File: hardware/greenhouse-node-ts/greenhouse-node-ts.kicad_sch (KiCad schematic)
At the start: 31 parts, among them J1 Conn_01x12_Male, J3 Conn_01x02_Pin, J7 Conn_01x04_Pin, SW1 SW_Push, U5 STM32F030F4P6, U7 PCF8574ATS/3,118, U8 XC6706x, U9 RFM69HW

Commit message: Tweaks to nodes
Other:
- moved on the sheet: AE1, C1, C10, C13, C14, C15, C16, D10, D6, D7, D8, D9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

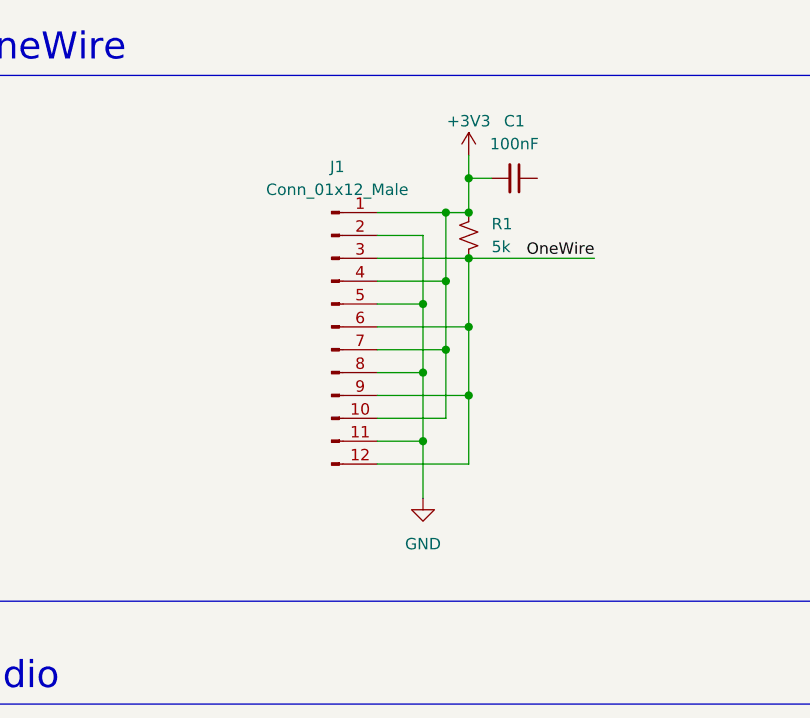
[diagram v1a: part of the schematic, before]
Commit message: Fixed cap sizes, generated BOMs
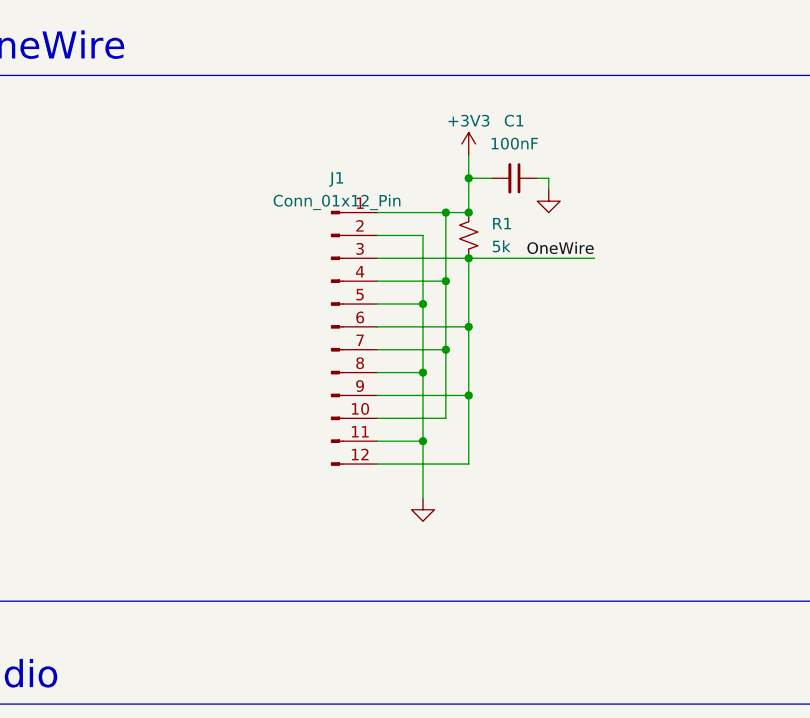
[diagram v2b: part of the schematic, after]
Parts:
- C14, C16: footprint Capacitor_THT:C_Disc_D4.7mm_W2.5mm_P5.00mm -> Capacitor_THT:C_Disc_D3.0mm_W2.0mm_P2.50mm
- J1: value Conn_01x12_Male -> Conn_01x12_Pin; footprint Connector_JST:JST_PH_B12B-PH-K_1x12_P2.00mm_Vertical -> (none); symbol Connector:Conn_01x12_Male -> Connector:Conn_01x12_Pin
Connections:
- net GND: now also C1.1
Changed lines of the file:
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@@
+    (stroke (width 0) (type default))
+  )
+  (wire (pts (xy 287.02 64.77) (xy 287.02 66.04))
     (stroke (width 0) (type default))
   )
@@
   )
   (wire (pts (xy 294.64 146.05) (xy 285.75 146.05))
+    (stroke (width 0) (type default))
+  )
+  (wire (pts (xy 285.75 64.77) (xy 287.02 64.77))
     (stroke (width 0) (type default))
   )
@@
     )
   )
-  (symbol (lib_id "power:GND") (at 273.05 100.33 0) (unit 1)
+  (symbol (lib_id "Nick:GND") (at 273.05 100.33 0) (unit 1)
     (in_bom yes) (on_board yes) (dnp no) (fields_autoplaced)
     (property "Reference" "#PWR01" (at 273.05 106.68 0)
@@
     )
     (property "Value" "GND" (at 273.05 105.41 0)
-      (effects (font (size 1.27 1.27)))
+      (effects (font (size 1.27 1.27)) hide)
     )
     (property "Footprint" "" (at 273.05 100.33 0)
@@
       (effects (font (size 1.27 1.27)))
     )
-    (property "Footprint" "Capacitor_THT:C_Disc_D4.7mm_W2.5mm_P5.00mm" (at 166.37 142.24 0)
+    (property "Footprint" "Capacitor_THT:C_Disc_D3.0mm_W2.0mm_P2.50mm" (at 166.37 142.24 0)
       (effects (font (size 1.27 1.27)) hide)
     )
@@
         (path "/d6d8dcc8-67cc-42c5-89b4-d76037b5248a"
           (reference "H4") (unit 1)
+        )
+      )
+    )
+  )
+  (symbol (lib_id "Nick:GND") (at 287.02 66.04 0) (unit 1)
+    (in_bom yes) (on_board yes) (dnp no) (fields_autoplaced)
+    (property "Reference" "#PWR05" (at 287.02 72.39 0)
+      (effects (font (size 1.27 1.27)) hide)
+    )
+    (property "Value" "GND" (at 287.02 71.12 0)
+      (effects (font (size 1.27 1.27)) hide)
+    )
+    (property "Footprint" "" (at 287.02 66.04 0)
+      (effects (font (size 1.27 1.27)) hide)
+    )
+    (property "Datasheet" "" (at 287.02 66.04 0)
+      (effects (font (size 1.27 1.27)) hide)
+    )
+    (pin "1")
+    (instances
+      (project "greenhouse-node-ts"
+        (path "/d6d8dcc8-67cc-42c5-89b4-d76037b5248a"
+          (reference "#PWR05") (unit 1)
         )
       )
@@
     )
   )
-  (symbol (lib_id "power:GND") (at 297.18 143.51 0) (unit 1)
+  (symbol (lib_id "Nick:GND") (at 297.18 143.51 0) (unit 1)
     (in_bom yes) (on_board yes) (dnp no) (fields_autoplaced)
     (property "Reference" "#PWR030" (at 297.18 149.86 0)
@@
       (effects (font (size 1.27 1.27)) hide)
     )
-    (property "Value" "GND" (at 124.46 231.1399 0)
-      (effects (font (size 1.27 1.27)) (justify left) hide)
+    (property "Value" "GND" (at 121.92 234.95 0)
+      (effects (font (size 1.27 1.27)) hide)
     )
     (property "Footprint" "" (at 121.92 229.87 0)
@@
       (effects (font (size 1.27 1.27)))
     )
-    (property "Footprint" "Capacitor_THT:C_Disc_D4.7mm_W2.5mm_P5.00mm" (at 266.7 137.16 0)
+    (property "Footprint" "Capacitor_THT:C_Disc_D3.0mm_W2.0mm_P2.50mm" (at 266.7 137.16 0)
       (effects (font (size 1.27 1.27)) hide)
     )
@@
     )
   )
-  (symbol (lib_id "Connector:Conn_01x12_Male") (at 262.89 81.28 0) (unit 1)
-    (in_bom yes) (on_board yes) (dnp no) (fields_autoplaced)
-    (property "Reference" "J1" (at 263.525 63.5 0)
-      (effects (font (size 1.27 1.27)))
-    )
-    (property "Value" "Conn_01x12_Male" (at 263.525 66.04 0)
-      (effects (font (size 1.27 1.27)))
-    )
-    (property "Footprint" "Connector_JST:JST_PH_B12B-PH-K_1x12_P2.00mm_Vertical" (at 262.89 81.28 0)
-      (effects (font (size 1.27 1.27)) hide)
-    )
+  (symbol (lib_id "Connector:Conn_01x12_Pin") (at 262.89 81.28 0) (unit 1)
+    (in_bom yes) (on_board yes) (dnp no) (fields_autoplaced)
+    (property "Reference" "J1" (at 263.525 64.77 0)
+      (effects (font (size 1.27 1.27)))
+    )
+    (property "Value" "Conn_01x12_Pin" (at 263.525 67.31 0)
+      (effects (font (size 1.27 1.27)))
+    )
+    (property "Footprint" "" (at 262.89 81.28 0)
+      (effects (font (size 1.27 1.27)) hide)
+    )

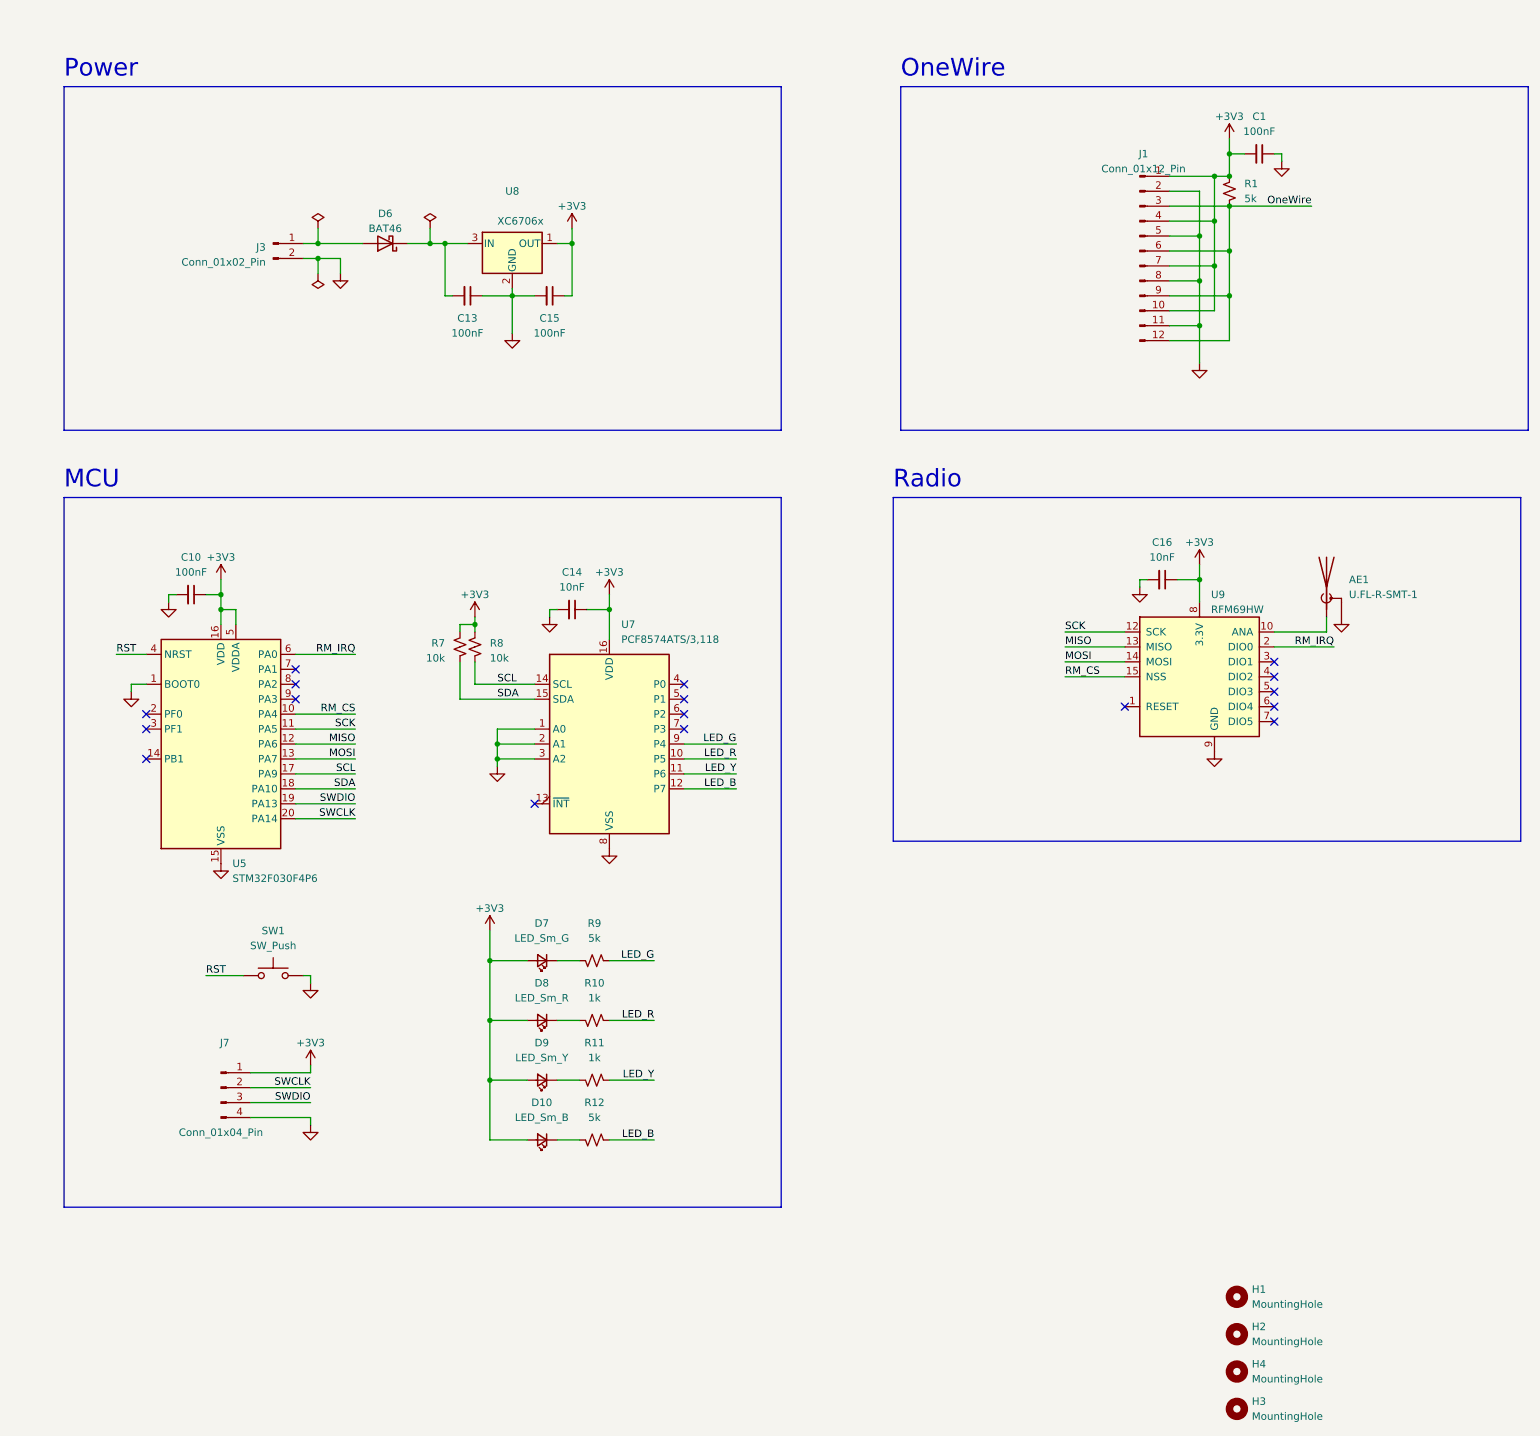
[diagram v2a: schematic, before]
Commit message: Improved schematics
Add todos, test points, fixed PCF8574 symbol,
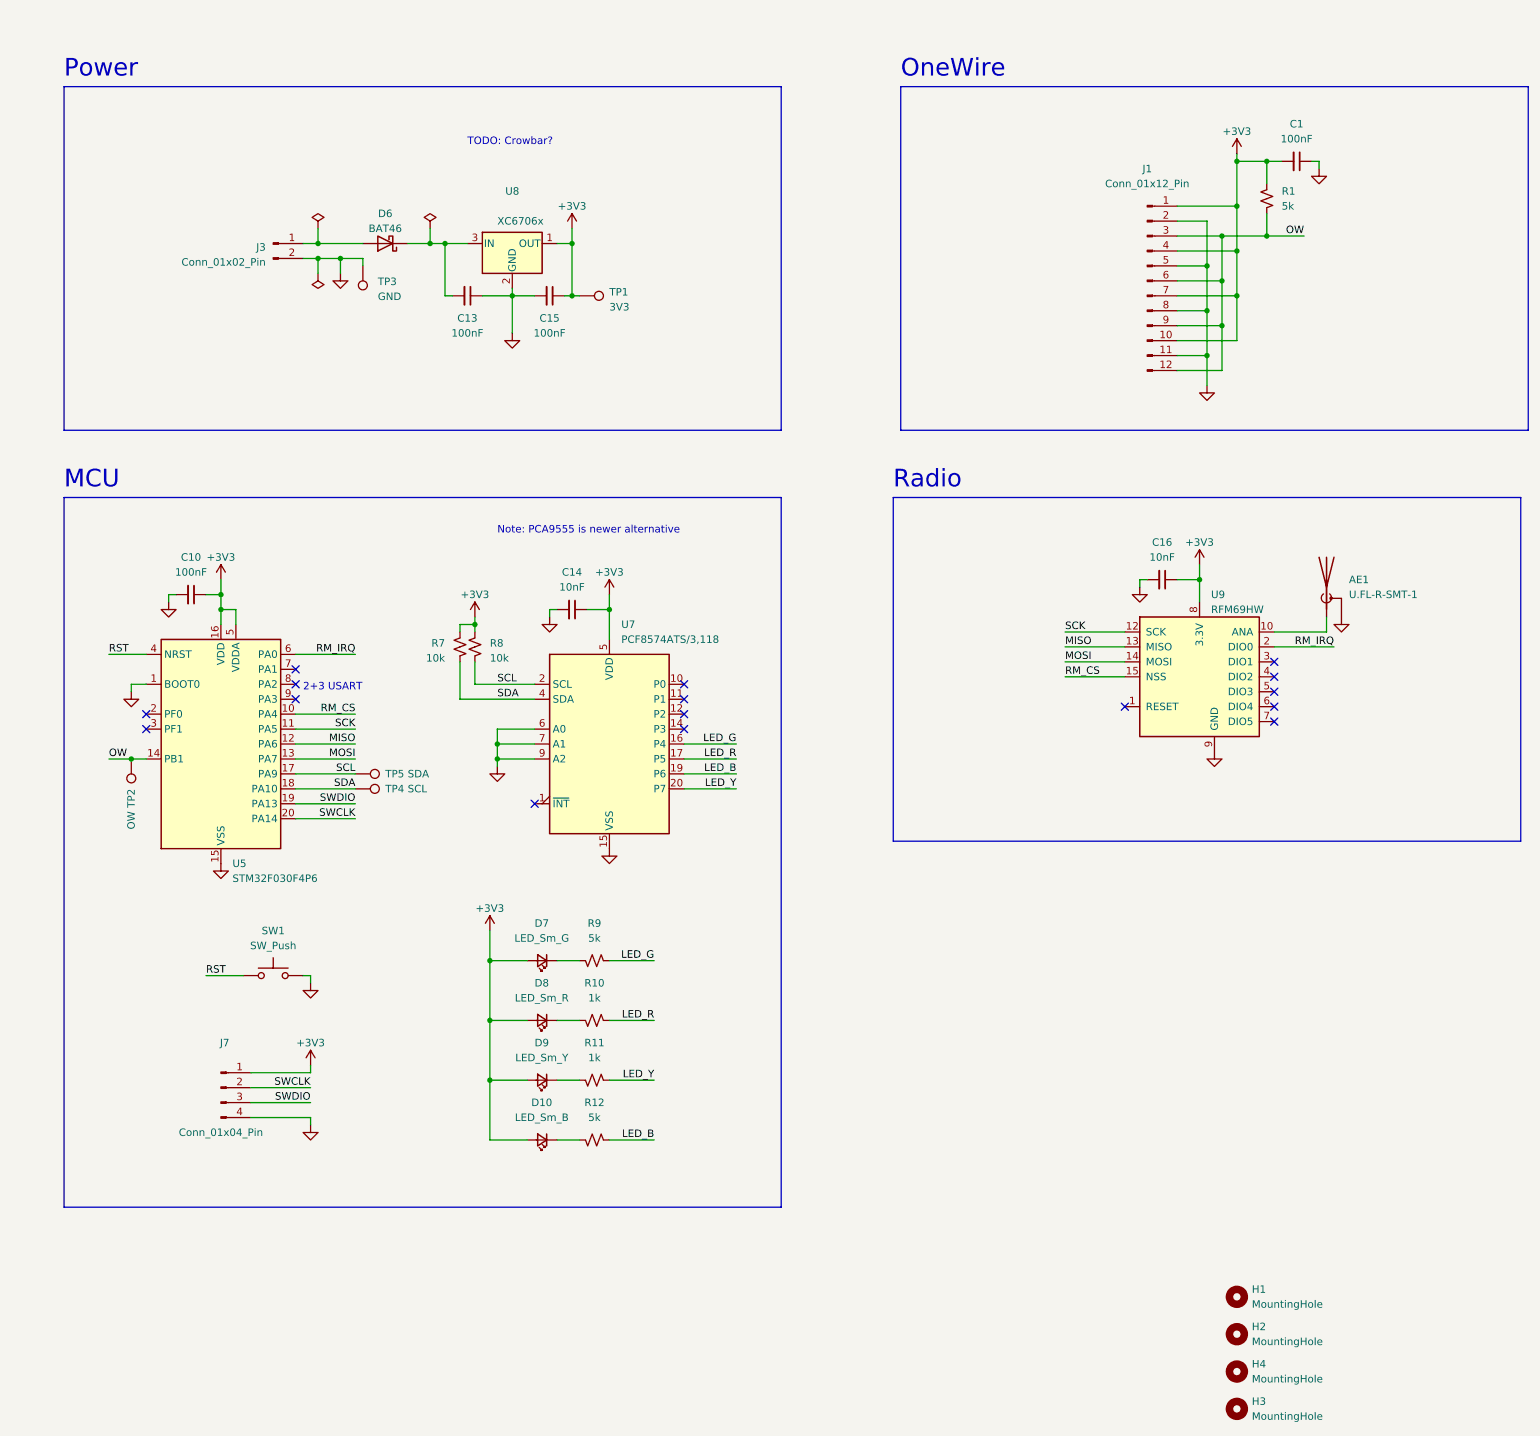
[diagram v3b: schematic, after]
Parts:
- added TP1: 3V3, TestPoint:TestPoint_Keystone_5019_Minature, symbol Connector:TestPoint
- added TP2: OW, TestPoint:TestPoint_Keystone_5019_Minature, symbol Connector:TestPoint
- added TP3: GND, TestPoint:TestPoint_Keystone_5019_Minature, symbol Connector:TestPoint
- added TP4: SCL, TestPoint:TestPoint_Keystone_5019_Minature, symbol Connector:TestPoint
- added TP5: SDA, TestPoint:TestPoint_Keystone_5019_Minature, symbol Connector:TestPoint
- J1: footprint (none) -> Connector_JST:JST_PH_B12B-PH-K_1x12_P2.00mm_Vertical
- U7: symbol Interface_Expansion:PCF8574 -> Interface_Expansion:PCF8574ATS
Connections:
- net OneWire is gone; now on net OW: J1.12 (Pin_12), J1.3 (Pin_3), J1.6 (Pin_6), J1.9 (Pin_9), R1.2
- net +3V3: now also U7.5 (VDD), TP1.1; no longer U7.16 (VDD)
- net GND: now also U7.15 (VSS), U7.6 (A0), U7.7 (A1), U7.9 (A2), TP3.1; no longer U7.1 (A0), U7.2 (A1), U7.3 (A2), U7.8 (VSS)
- net LED_B: now also U7.19 (P6); no longer U7.12 (P7)
- net LED_G: now also U7.16 (P4); no longer U7.9 (P4)
- net LED_R: now also U7.17 (P5); no longer U7.10 (P5)
- net LED_Y: now also U7.20 (P7); no longer U7.11 (P6)
- net SCL: now also U7.2 (SCL), TP5.1; no longer U7.14 (SCL)
- net SDA: now also U7.4 (SDA), TP4.1; no longer U7.15 (SDA)
- net OW: now reaches U5.14 (PB1)
- net OW: now also TP2.1
- no-connect marks 17 -> 16
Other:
- note added: "2+3 USART"
- note added: "Note: PCA9555 is newer alternative"
- note added: "TODO: Crowbar?"
- moved on the sheet: C1, J1, R1
